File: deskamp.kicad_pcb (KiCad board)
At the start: 2 copper layers, 33 parts, among them J1 Input 01, J2 Input 02, J3 Preamp Out, J4 Selector Switch, J5 LFE, J6 Mute, J7 Sleep, J8 Motor, J9 Power, K1 TQ2-12V, K2 TQ2-12V, K3 TQ2-12V, K4 TQ2-12V, Q1 PN2222A, Q2 PN2222A, Q3 PN2222A, Q4 PN2222A, U1 esp32-wemos-d1-mini, U2 L9110, U3 TSR_1-2433

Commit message: Update deskamp.kicad_pcb
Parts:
- moved J4 1.19 mm to (126.1, 90.6)
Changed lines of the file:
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@@
 	(footprint "Connector_JST:JST_XH_B3B-XH-AM_1x03_P2.50mm_Vertical"
 		(layer "F.Cu")
-		(at 126.5 91.725 180)
+		(at 126.1 90.6 180)
 		(descr "JST XH series connector, B3B-XH-AM, with boss (http://www.jst-mfg.com/product/pdf/eng/eXH.pdf), generated with kicad-footprint-generator")
 		(tags "connector JST XH vertical boss")
@@
 		(layer "F.Cu")
 		(net 11)
-	)
-	(segment
-		(start 126.4 88.81)
-		(end 126.3 88.91)
-		(width 0.2)
-		(layer "F.Cu")
-		(net 11)

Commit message: Update deskamp.kicad_pcb
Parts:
- moved U2 47.6 mm to (126.2, 94.8), turned to 180 degrees
- moved J4 44.8 mm to (170.8, 92.1)
- moved J8 37.1 mm to (129.8, 77.8)
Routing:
- net GND: track 74.3 -> 179.7 mm
- net GNDA: track 64.2 -> 129.0 mm
- net Net-(U1-IO_04): track 41.6 -> 1.50 mm
- net Net-(U1-IO_00): track 40.7 -> 1.84 mm
- net +3V3: track 65.5 -> 51.4 mm
- net Net-(J8-Pin_1): track 13.1 -> 18.5 mm
- net Net-(J8-Pin_2): track 11.0 -> 9.88 mm

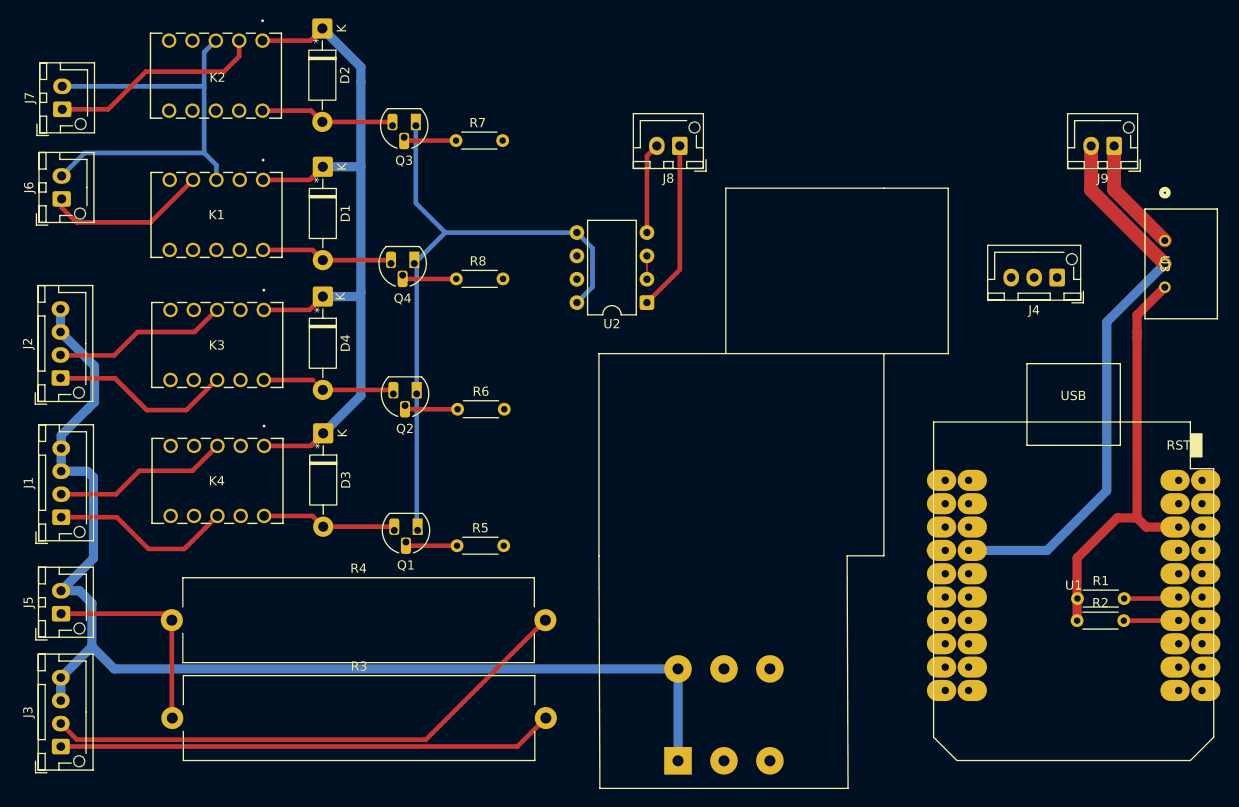
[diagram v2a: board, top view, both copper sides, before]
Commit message: Start routing signals
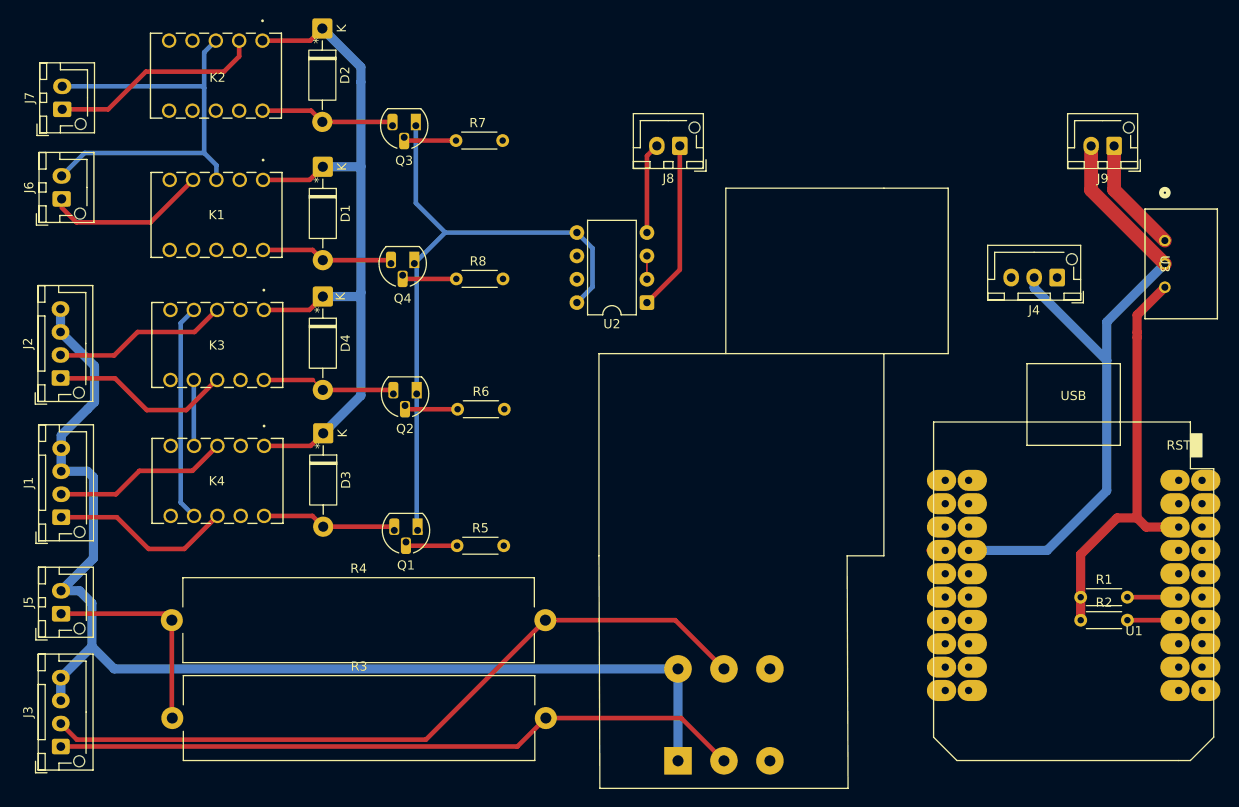
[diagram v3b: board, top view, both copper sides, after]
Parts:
- moved R2 0.39 mm to (173.4, 129.3)
- moved R1 0.38 mm to (173.4, 126.8)
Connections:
- RV1 pad 2: Net-(J3-Pin_2) -> Net-(J3-Pin_1)
- RV1 pad 5: Net-(J3-Pin_1) -> Net-(J3-Pin_2)
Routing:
- net Net-(K3-Pad7): track 0.00 -> 23.6 mm
- net Net-(J3-Pin_2): track 58.8 -> 80.5 mm
- net Net-(J3-Pin_1): track 54.1 -> 75.4 mm
- net GND: track 179.7 -> 192.0 mm
- net Net-(K3-Pad4): track 0.00 -> 7.18 mm
- net +3V3: track 51.4 -> 48.8 mm
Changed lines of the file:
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@@
 		(at 172.645 125.57 180)
 		(property "Reference" "U1"
-			(at 0 0 0)
+			(at -6.57 -4.96 180)
 			(layer "F.SilkS")
 			(effects
@@
 	(footprint "Resistor_THT:R_Axial_DIN0204_L3.6mm_D1.6mm_P5.08mm_Horizontal"
 		(layer "F.Cu")
-		(at 173.06 127)
+		(at 173.41 126.85)
 		(descr "Resistor, Axial_DIN0204 series, Axial, Horizontal, pin pitch=5.08mm, 0.167W, length*diameter=3.6*1.6mm^2, http://cdn-reichelt.de/documents/datenblatt/B400/1_4W%23YAG.pdf")
 		(tags "Resistor Axial_DIN0204 series Axial Horizontal pin pitch 5.08mm 0.167W length 3.6mm diameter 1.6mm")
@@
 	(footprint "Resistor_THT:R_Axial_DIN0204_L3.6mm_D1.6mm_P5.08mm_Horizontal"
 		(layer "F.Cu")
-		(at 173.02 129.4)
+		(at 173.41 129.35)
 		(descr "Resistor, Axial_DIN0204 series, Axial, Horizontal, pin pitch=5.08mm, 0.167W, length*diameter=3.6*1.6mm^2, http://cdn-reichelt.de/documents/datenblatt/B400/1_4W%23YAG.pdf")
 		(tags "Resistor Axial_DIN0204 series Axial Horizontal pin pitch 5.08mm 0.167W length 3.6mm diameter 1.6mm")
@@
 			(layers "*.Cu" "*.Mask")
 			(remove_unused_layers no)
-			(net 79 "Net-(J3-Pin_2)")
+			(net 80 "Net-(J3-Pin_1)")
 			(pinfunction "2")
 			(pintype "passive")
@@
 			(layers "*.Cu" "*.Mask")
 			(remove_unused_layers no)
-			(net 80 "Net-(J3-Pin_1)")
+			(net 79 "Net-(J3-Pin_2)")
 			(pinfunction "5")
 			(pintype "passive")
@@
 	)
 	(segment
-		(start 178.1 129.4)
-		(end 184.055 129.4)
+		(start 184.045 129.35)
+		(end 178.49 129.35)
 		(width 0.5)
 		(layer "F.Cu")
@@
 	)
 	(segment
+		(start 184.075 129.38)
+		(end 184.045 129.35)
+		(width 0.2)
+		(layer "F.Cu")
+		(net 11)
+	)
+	(segment
 		(start 184.055 129.4)
 		(end 184.075 129.38)
@@
 	)
 	(segment
+		(start 176.245 101.1)
+		(end 168.35 93.205)
+		(width 1)
+		(layer "B.Cu")
+		(net 12)
+	)
+	(segment
 		(start 77.87 71.27)
 		(end 78.05 71.45)
@@
 	)
 	(segment
+		(start 168.35 93.205)
+		(end 168.35 92.075)
+		(width 1)
+		(layer "B.Cu")
+		(net 12)
+	)
+	(segment
 		(start 78.05 78.521325)
 		(end 78.05 71.45)
@@
 	)
 	(segment
-		(start 176.245 115.27)
+		(start 176.245 101.1)
 		(end 176.245 96.9)
 		(width 1)
@@
 	)
 	(segment
+		(start 176.245 115.27)
+		(end 176.245 101.1)
+		(width 1)
+		(layer "B.Cu")
+		(net 12)
+	)
+	(segment
 		(start 101.17 119.48)
 		(end 101.27 119.58)
@@
 	)
 	(segment
+		(start 76.92 110.3596)
+		(end 76.9473 110.3869)
+		(width 0.2)
+		(layer "B.Cu")
+		(net 20)
+	)
+	(segment
+		(start 76.92 103.22)
+		(end 76.92 110.3596)
+		(width 0.5)
+		(layer "B.Cu")
+		(net 20)
+	)
+	(segment
+		(start 76.92 95.6)
+		(end 75.4957 97.0243)
+		(width 0.5)
+		(layer "B.Cu")
+		(net 21)
+	)
+	(segment
+		(start 75.4957 97.0243)
+		(end 75.4957 116.5553)
+		(width 0.5)
+		(layer "B.Cu")
+		(net 21)
+	)
+	(segment
+		(start 75.4957 116.5553)
+		(end 76.9473 118.0069)
+		(width 0.5)
+		(layer "B.Cu")
+		(net 21)
+	)
+	(segment
 		(start 100.4 121.25)
 		(end 100 120.85)
@@
 	)
 	(segment
-		(start 177.37 118.23)
-		(end 173.02 122.58)
-		(width 1)
-		(layer "F.Cu")
-		(net 31)
-	)
-	(segment
-		(start 173.02 127.04)
-		(end 173.06 127)
+		(start 173.37 129.11)
+		(end 173.33 129.15)
 		(width 0.2)
 		(layer "F.Cu")
@@
 	)
 	(segment
+		(start 173.41 122.23)
+		(end 173.41 129.35)
+		(width 1)
+		(layer "F.Cu")
+		(net 31)
+	)
+	(segment
 		(start 126.22 89.72)
 		(end 126.22 92.26)
@@
 	)
 	(segment
-		(start 179.545 118.23)
-		(end 180.535 119.22)
+		(start 173.39 122.21)
+		(end 173.41 122.23)
 		(width 1)
 		(layer "F.Cu")
@@
 	)
 	(segment
-		(start 173.02 129.4)
-		(end 173.02 127.04)
-		(width 0.2)
+		(start 179.545 118.23)
+		(end 180.535 119.22)
+		(width 1)
 		(layer "F.Cu")
 		(net 31)
 	)
 	(segment
-		(start 179.545 98.57)
-		(end 179.545 118.23)
+		(start 177.37 118.23)
+		(end 173.39 122.21)
 		(width 1)
 		(layer "F.Cu")
@@
 	)
 	(segment
-		(start 173.02 122.58)
-		(end 173.02 129.4)
+		(start 179.545 98.57)
+		(end 179.545 118.23)
 		(width 1)
 		(layer "F.Cu")
@@
 	)
 	(segment
-		(start 178.14 127)
-		(end 183.915 127)
+		(start 184.065 126.85)
+		(end 178.49 126.85)
 		(width 0.5)
 		(layer "F.Cu")
@@
 	)
 	(segment
+		(start 184.075 126.84)
+		(end 184.065 126.85)
+		(width 0.2)
+		(layer "F.Cu")
+		(net 78)
+	)
+	(segment
 		(start 62.45 140.6)
 		(end 64.2 142.35)
@@
 	)
 	(segment
+		(start 129.3 129.35)
+		(end 115.17 129.35)
+		(width 0.5)
+		(layer "F.Cu")
+		(net 79)
+	)
+	(segment
 		(start 102.17 142.35)
 		(end 115.17 129.35)
@@
 	)
 	(segment
+		(start 134.6 134.65)
+		(end 129.3 129.35)
+		(width 0.5)
+		(layer "F.Cu")
+		(net 79)
+	)
+	(segment
 		(start 62.45 143.1)
 		(end 112.12 143.1)
@@
 	)
 	(segment
+		(start 129.95 140)
+		(end 115.22 140)
+		(width 0.5)
+		(layer "F.Cu")
+		(net 80)
+	)
+	(segment
 		(start 112.12 143.1)
 		(end 115.22 140)
 		(width 0.5)
 		(layer "F.Cu")
+		(net 80)
+	)
+	(segment
+		(start 134.6 144.65)
+		(end 129.95 140)
+		(width 0.5)
+		(layer "F.Cu")

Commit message: Update deskamp.kicad_pcb
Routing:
- net +3V3: track 48.8 -> 104.8 mm
- net Net-(J4-Pin_3): track 5.82 -> 12.5 mm
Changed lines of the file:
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@@
 		(start 126.22 94.8)
 		(end 129.8 91.22)
-		(width 0.5)
-		(layer "F.Cu")
+		(width 1)
+		(layer "B.Cu")
 		(net 15)
 	)
@@
 		(start 129.8 91.22)
 		(end 129.8 77.75)
-		(width 0.5)
-		(layer "F.Cu")
+		(width 1)
+		(layer "B.Cu")
 		(net 15)
 	)
@@
 		(start 126.22 87.18)
 		(end 126.22 78.83)
-		(width 0.5)
+		(width 1)
 		(layer "F.Cu")
 		(net 16)
@@
 		(start 126.22 78.83)
 		(end 127.3 77.75)
-		(width 0.5)
+		(width 1)
 		(layer "F.Cu")
 		(net 16)
@@
 	)
 	(segment
+		(start 126.22 92.26)
+		(end 132.69 92.26)
+		(width 1)
+		(layer "F.Cu")
+		(net 31)
+	)
+	(segment
 		(start 126.22 89.72)
 		(end 126.22 92.26)
-		(width 0.2)
+		(width 1)
 		(layer "F.Cu")
 		(net 31)
@@
 	)
 	(segment
+		(start 139 98.57)
+		(end 179.545 98.57)
+		(width 1)
+		(layer "F.Cu")
+		(net 31)
+	)
+	(segment
 		(start 179.545 118.23)
 		(end 180.535 119.22)
@@
 	)
 	(segment
+		(start 132.69 92.26)
+		(end 139 98.57)
+		(width 1)
+		(layer "F.Cu")
+		(net 31)
+	)
+	(segment
 		(start 158.312976 124.3)
 		(end 158.675 124.3)
@@
 	)
 	(segment
+		(start 178.49 126.85)
+		(end 176.4 128.94)
+		(width 0.5)
+		(layer "F.Cu")
+		(net 78)
+	)
+	(segment
 		(start 184.075 126.84)
 		(end 184.065 126.85)
@@
 		(layer "F.Cu")
 		(net 78)
+	)
+	(segment
+		(start 176.4 128.94)
+		(end 176.4 132.7)
+		(width 0.5)
+		(layer "F.Cu")
+		(net 78)

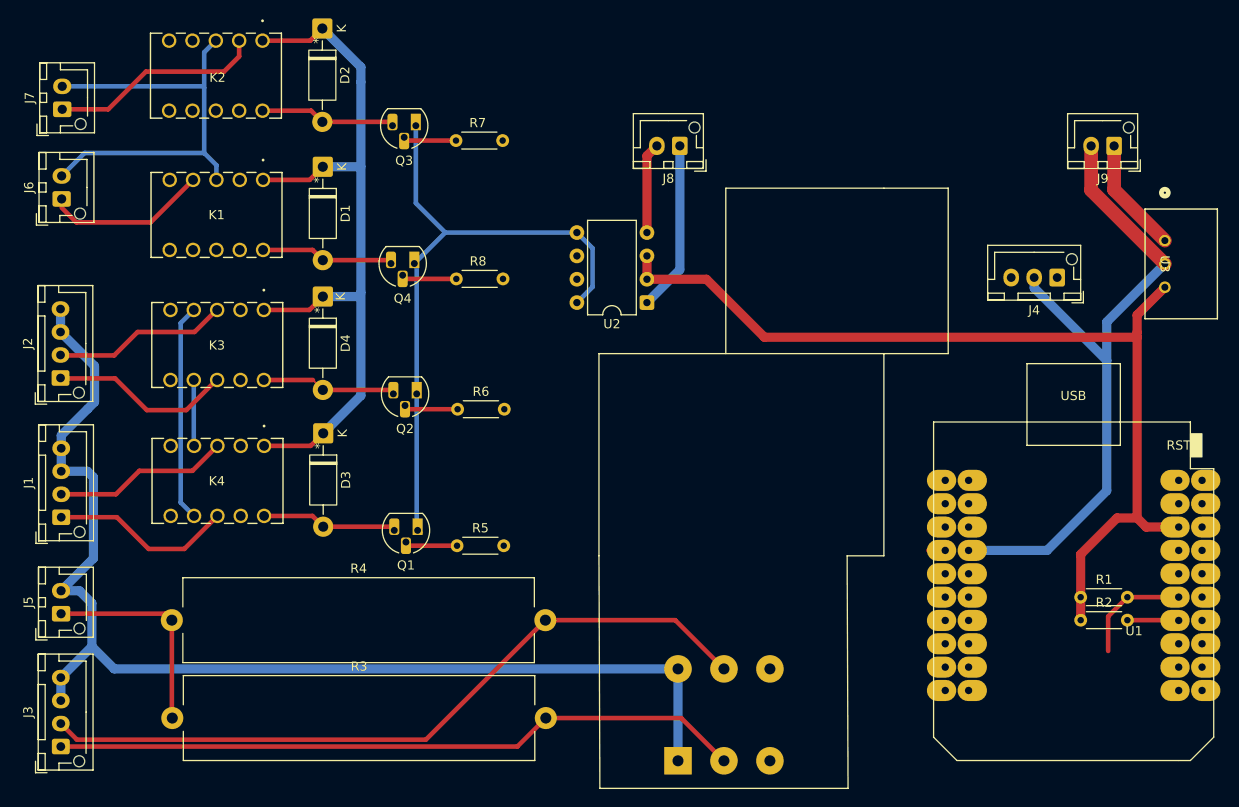
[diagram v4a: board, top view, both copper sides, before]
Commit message: Add mute selector pulldown
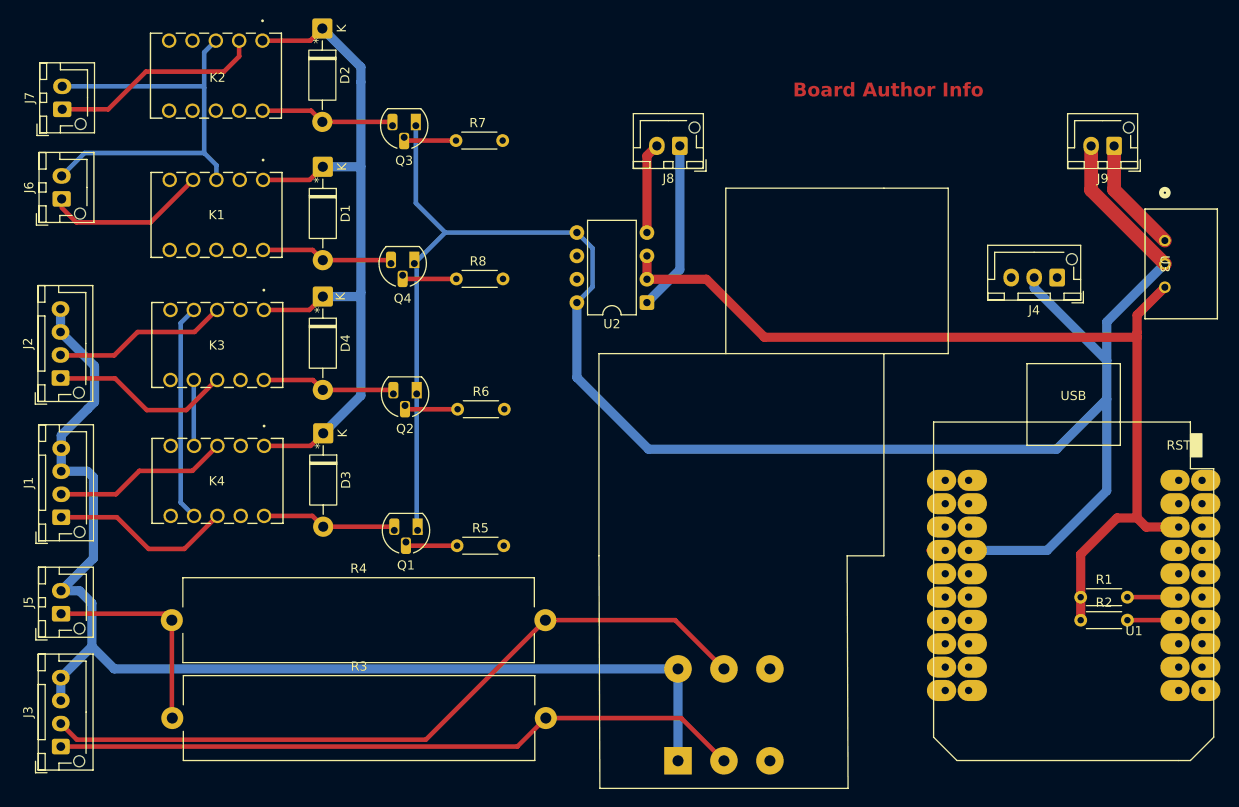
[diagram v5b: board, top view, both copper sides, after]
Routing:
- net GND: track 192.0 -> 263.3 mm
- net Net-(J4-Pin_3): track 12.5 -> 5.82 mm
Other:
- board text added: "Board Author Info"
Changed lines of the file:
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@@
 		(layer "Margin")
+	)
+	(gr_text "Board Author Info"
+		(at 142.1 72.55 0)
+		(layer "F.Cu")
+		(effects
+			(font
+				(size 1.5 1.5)
+				(thickness 0.3)
+				(bold yes)
+			)
+			(justify left bottom)
+		)
 	)
 	(segment
@@
 		(start 89.88 103.22)
 		(end 90.96 104.3)
-		(width 0.2)
+		(width 0.5)
 		(layer "F.Cu")
 		(net 5)
@@
 	)
 	(segment
+		(start 176.245 105.3)
+		(end 170.795 110.75)
+		(width 1)
+		(layer "B.Cu")
+		(net 12)
+	)
+	(segment
 		(start 118.6 87.18)
 		(end 120.3 88.88)
@@
 	)
 	(segment
+		(start 170.795 110.75)
+		(end 126.4 110.75)
+		(width 1)
+		(layer "B.Cu")
+		(net 12)
+	)
+	(segment
 		(start 104.2827 87.18)
 		(end 100.9127 90.55)
@@
 	)
 	(segment
-		(start 176.245 115.27)
+		(start 176.245 105.3)
 		(end 176.245 101.1)
 		(width 1)
@@
 	)
 	(segment
+		(start 176.245 115.27)
+		(end 176.245 105.3)
+		(width 1)
+		(layer "B.Cu")
+		(net 12)
+	)
+	(segment
 		(start 101.17 104.73)
 		(end 101.17 119.48)
@@
 	)
 	(segment
+		(start 126.4 110.75)
+		(end 118.6 102.95)
+		(width 1)
+		(layer "B.Cu")
+		(net 12)
+	)
+	(segment
+		(start 118.6 102.95)
+		(end 118.6 94.8)
+		(width 1)
+		(layer "B.Cu")
+		(net 12)
+	)
+	(segment
 		(start 118.6 87.18)
 		(end 104.2827 87.18)
@@
 	)
 	(segment
-		(start 178.49 126.85)
-		(end 176.4 128.94)
-		(width 0.5)
-		(layer "F.Cu")
-		(net 78)
-	)
-	(segment
 		(start 184.075 126.84)
 		(end 184.065 126.85)
@@
 		(layer "F.Cu")
 		(net 78)
-	)
-	(segment
-		(start 176.4 128.94)
-		(end 176.4 132.7)
-		(width 0.5)
-		(layer "F.Cu")
-		(net 78)

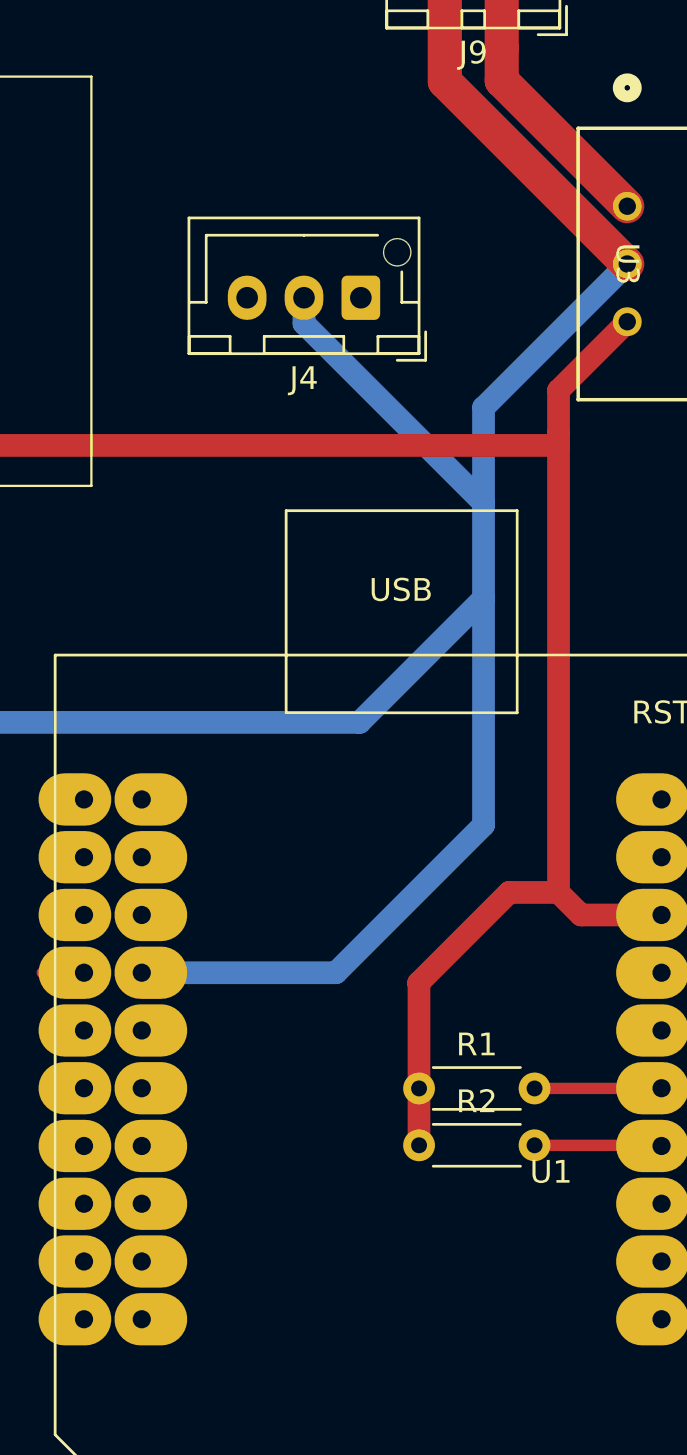
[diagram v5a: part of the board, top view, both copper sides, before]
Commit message: Update footprints
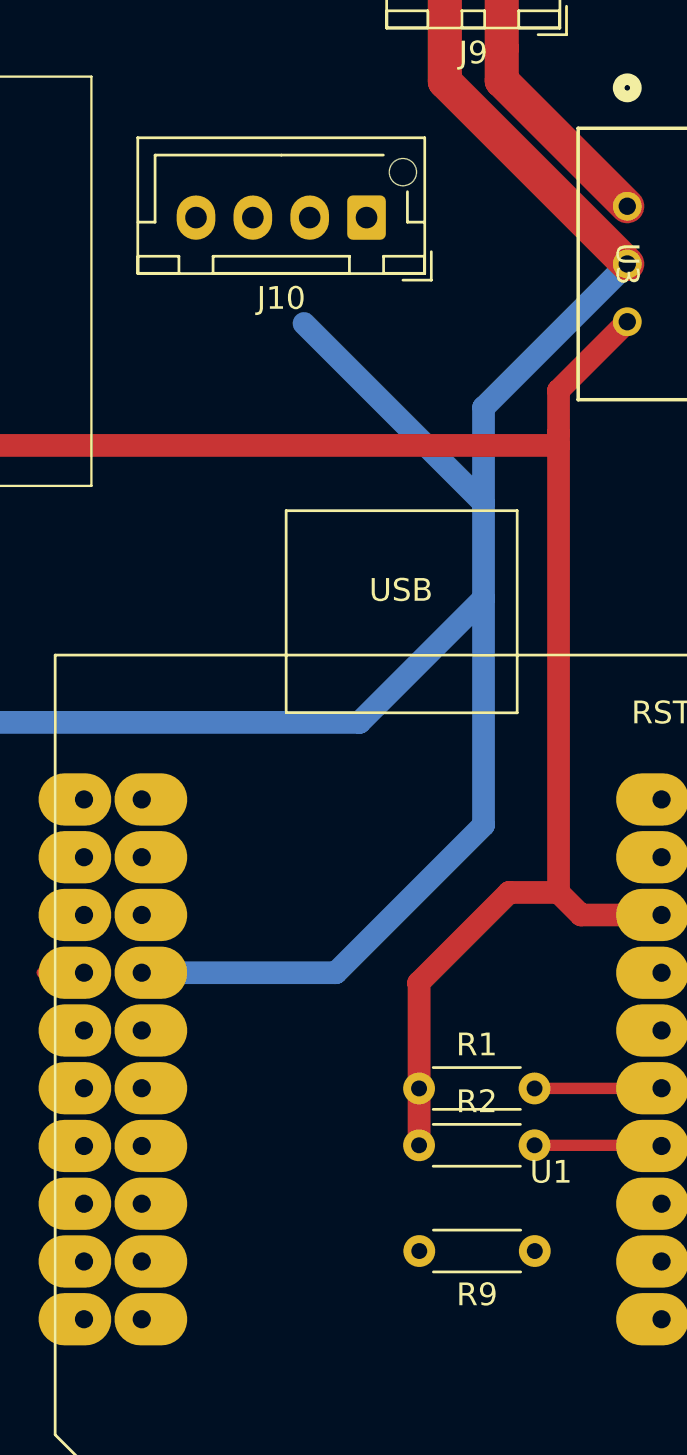
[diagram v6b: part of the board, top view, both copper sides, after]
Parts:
- removed J4: Selector Switch, Connector_JST:JST_XH_B3B-XH-AM_1x03_P2.50mm_Vertical
- added J10: Input Select, Connector_JST:JST_XH_B4B-XH-AM_1x04_P2.50mm_Vertical, F.Cu at (171.1, 88.5)
- added R9: 10K, Resistor_THT:R_Axial_DIN0204_L3.6mm_D1.6mm_P5.08mm_Horizontal, F.Cu at (178.5, 134.0)
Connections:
- U1 pad 28: unconnected-(U1-IO_32-Pad28) -> Net-(J10-Pin_2)
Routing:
- net GND: track 263.3 -> 262.2 mm
